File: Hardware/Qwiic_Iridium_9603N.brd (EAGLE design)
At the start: 50.8 x 50.8 mm, 92 parts, among them J1 IRIDIUM_9603N, J10 STANDOFFS_M2X0.4_STEEL_6MM, J3 PTH, J6 ISP, J7 U.FL, J9 STANDOFFS_M2X0.4_STEEL_6MM, Q2 5.8A/30V/35mΩ, U1 ATTINY841SOIC, U2 LTC3225EDDB#TRMPBF, U3 ADM4210-1

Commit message: Adding x02 regular and production files.
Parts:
- removed J10, J9: STANDOFFS_M2X0.4_STEEL_6MM, New_Parts:STANDOFF_M2X0.4
- C5, C6: device New_Parts:CPOL-RADIAL-1F-2.7V -> SparkFun-Capacitors:CPOL-RADIAL-1F-2.7V
- J1: device New_Parts:IRIDIUM_9603N -> Qwiic_Iridium_9603N:IRIDIUM_9603N
- R1, R12: device SparkFun-Resistors:0603 -> Qwiic_Iridium_9603N:0603
- R9: value 0.012R -> 0.012 Ohm; device New_Parts:0603 -> SparkFun-Resistors:0603
- U1: device New_Parts:ATTINY841 -> Qwiic_Iridium_9603N:ATTINY841
- U2: device New_Parts:DFN300X200-10L -> Qwiic_Iridium_9603N:DFN300X200-10L
- U3: device New_Parts:TSOT6 -> Qwiic_Iridium_9603N:TSOT6
- moved J1 27.5 mm to (12.7, 8.89)
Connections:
- net GND: now also J1.HOLE1, J1.HOLE2; no longer J10.1, J9.1

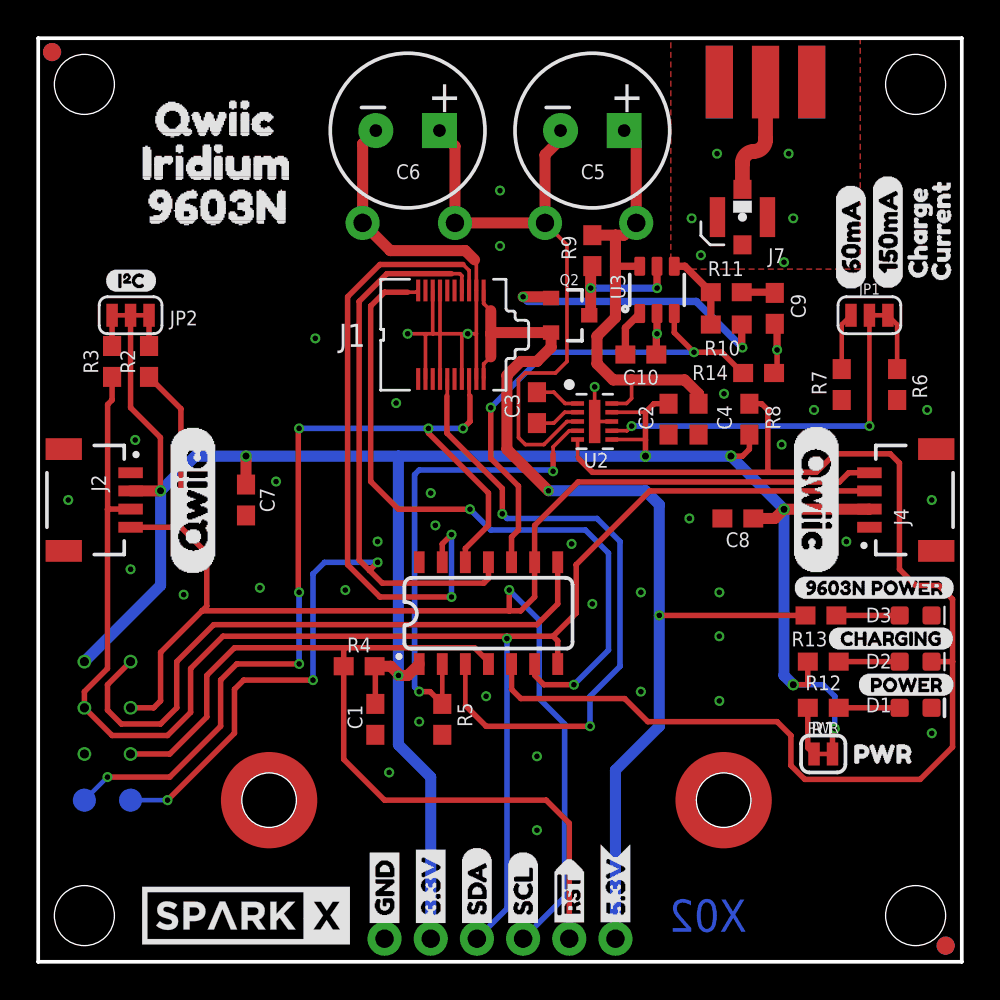
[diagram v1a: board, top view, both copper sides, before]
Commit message: X03 Candidate - adds standoffs as separate items for the BOM
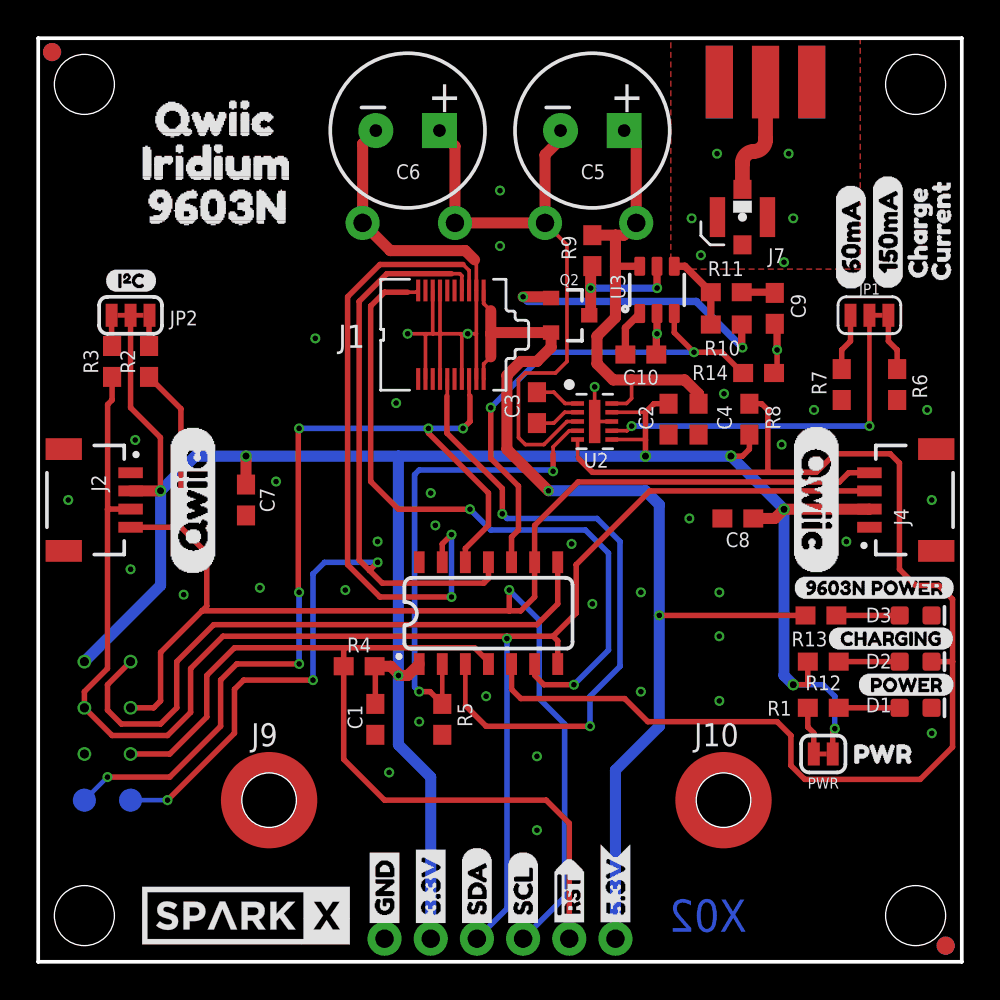
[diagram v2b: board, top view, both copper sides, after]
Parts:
- added J10, J9: STANDOFFS_M2X0.4_STEEL_6MM, New_Parts:STANDOFF_M2X0.4
- C5, C6: device SparkFun-Capacitors:CPOL-RADIAL-1F-2.7V -> New_Parts:CPOL-RADIAL-1F-2.7V
- J1: device Qwiic_Iridium_9603N:IRIDIUM_9603N -> New_Parts:IRIDIUM_9603N
- R1, R12: device Qwiic_Iridium_9603N:0603 -> SparkFun-Resistors:0603
- R9: value 0.012 Ohm -> 0.012R; device SparkFun-Resistors:0603 -> New_Parts:0603
- U1: device Qwiic_Iridium_9603N:ATTINY841 -> New_Parts:ATTINY841
- U2: device Qwiic_Iridium_9603N:DFN300X200-10L -> New_Parts:DFN300X200-10L
- U3: device Qwiic_Iridium_9603N:TSOT6 -> New_Parts:TSOT6
- moved J1 27.5 mm to (22.7, 34.5)
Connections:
- net GND: now also J10.1, J9.1; no longer J1.HOLE1, J1.HOLE2
